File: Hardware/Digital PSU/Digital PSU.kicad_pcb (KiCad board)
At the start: 2 copper layers, 35 parts, among them J1 ACin, J2 Relay power, J3 Conn_02x09, Q1 NJW0302, Q2 MJE15030, U1 LM334Z

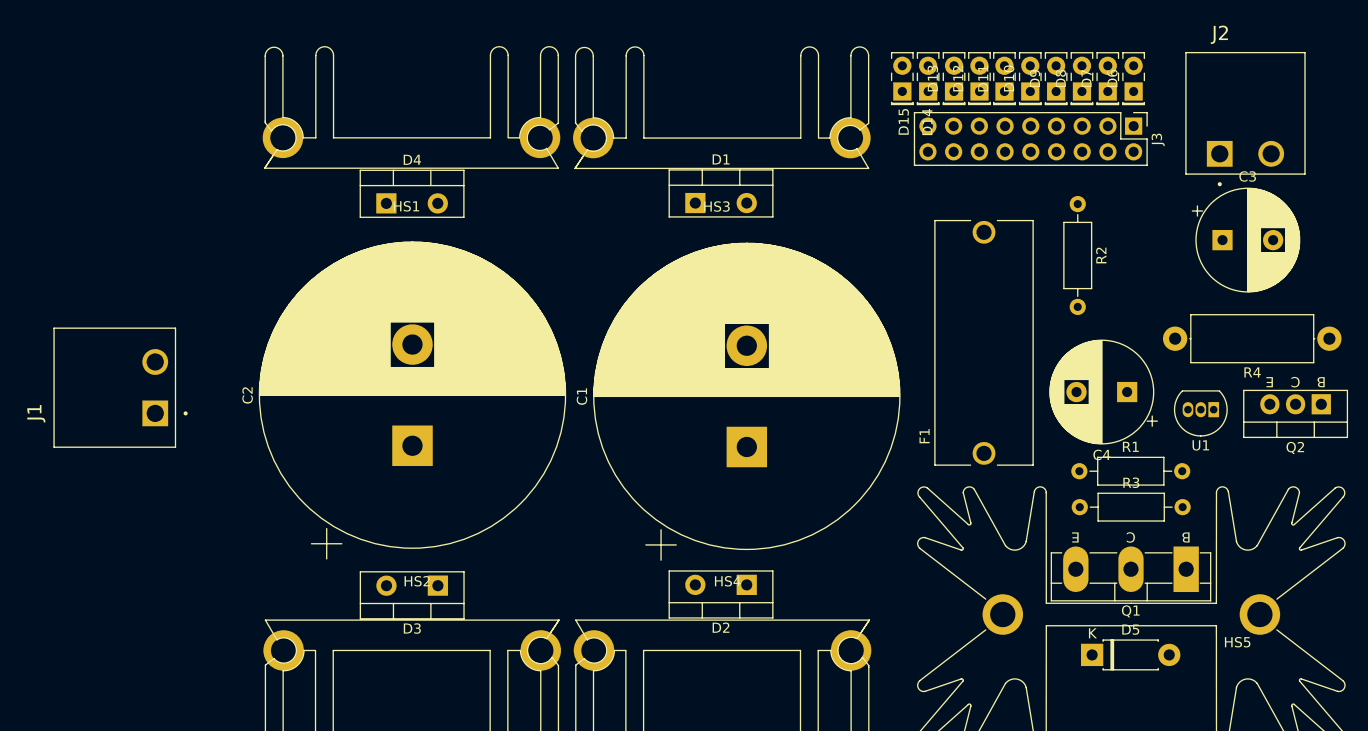
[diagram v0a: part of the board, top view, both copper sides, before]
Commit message: More work on PSU
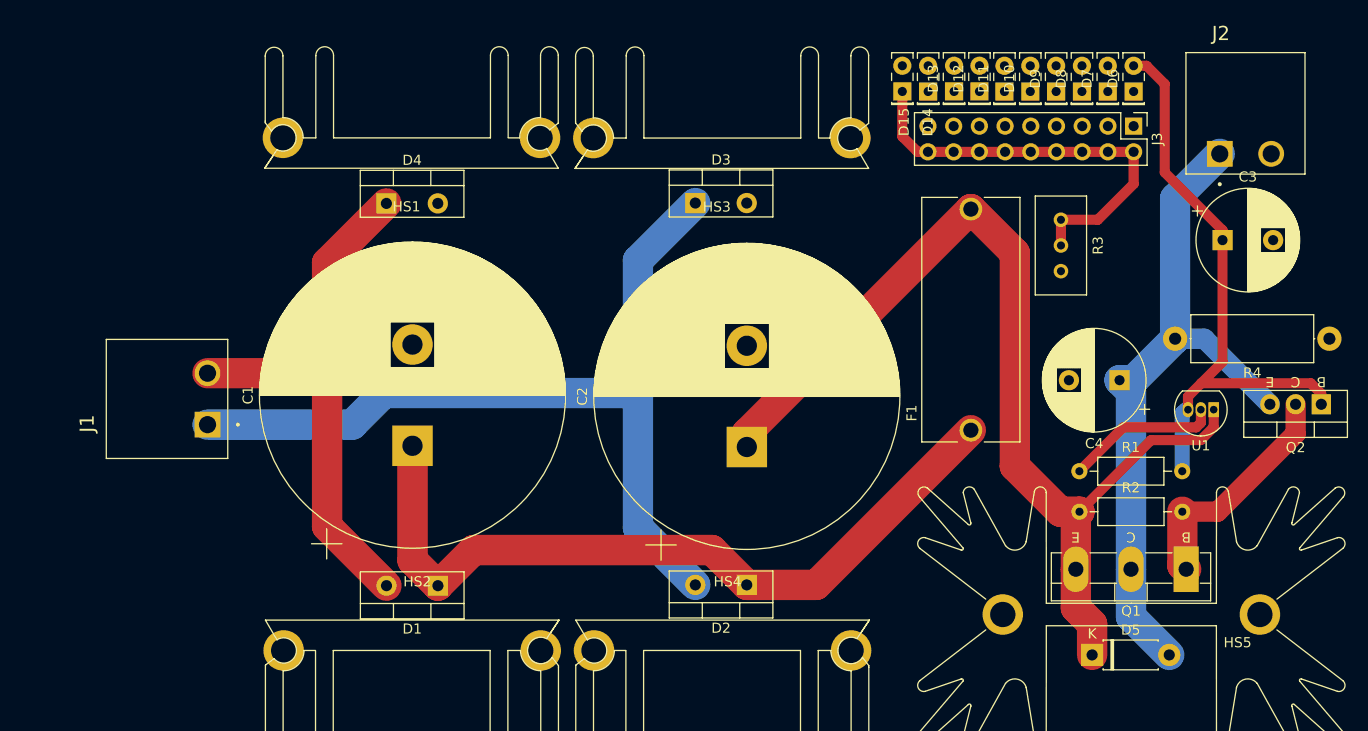
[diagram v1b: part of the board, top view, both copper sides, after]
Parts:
- R3: footprint Resistor_THT:R_Axial_DIN0207_L6.3mm_D2.5mm_P10.16mm_Horizontal -> Potentiometer_THT:Potentiometer_Bourns_3296W_Vertical
- moved D1 45.6 mm to (92.9, 165.8), turned to 180 degrees
- moved D3 45.6 mm to (118.3, 128.0), turned to 0 degrees
- moved C1 33.0 mm to (90.4, 152.0)
- moved C2 33.0 mm to (123.4, 152.1)
- moved R2 30.4 mm to (156.3, 158.5), turned to 0 degrees
- moved R3 23.4 mm to (154.4, 134.8), turned to -90 degrees
- moved J1 5.28 mm to (70.1, 149.9)
- moved F1 2.63 mm to (145.6, 139.6)
- moved C4 1.39 mm to (160.2, 145.5)
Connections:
- R3 pad 1: Net-(D15-K) -> GND
- R3 pad 2: GND -> Net-(D15-K)
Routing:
- net Net-(D5-K): track 0.00 -> 101.5 mm
- net Net-(D2-A): track 0.00 -> 86.2 mm
- net Net-(D1-K): track 0.00 -> 76.7 mm
- net +12V: track 0.00 -> 68.5 mm
- net Net-(D6-A): track 0.00 -> 59.3 mm
- net Net-(D1-A): track 0.00 -> 54.4 mm
- net Net-(D15-K): track 0.00 -> 42.3 mm
- net Net-(Q1-B): track 0.00 -> 23.1 mm
- net Net-(R1-Pad1): track 0.00 -> 15.3 mm

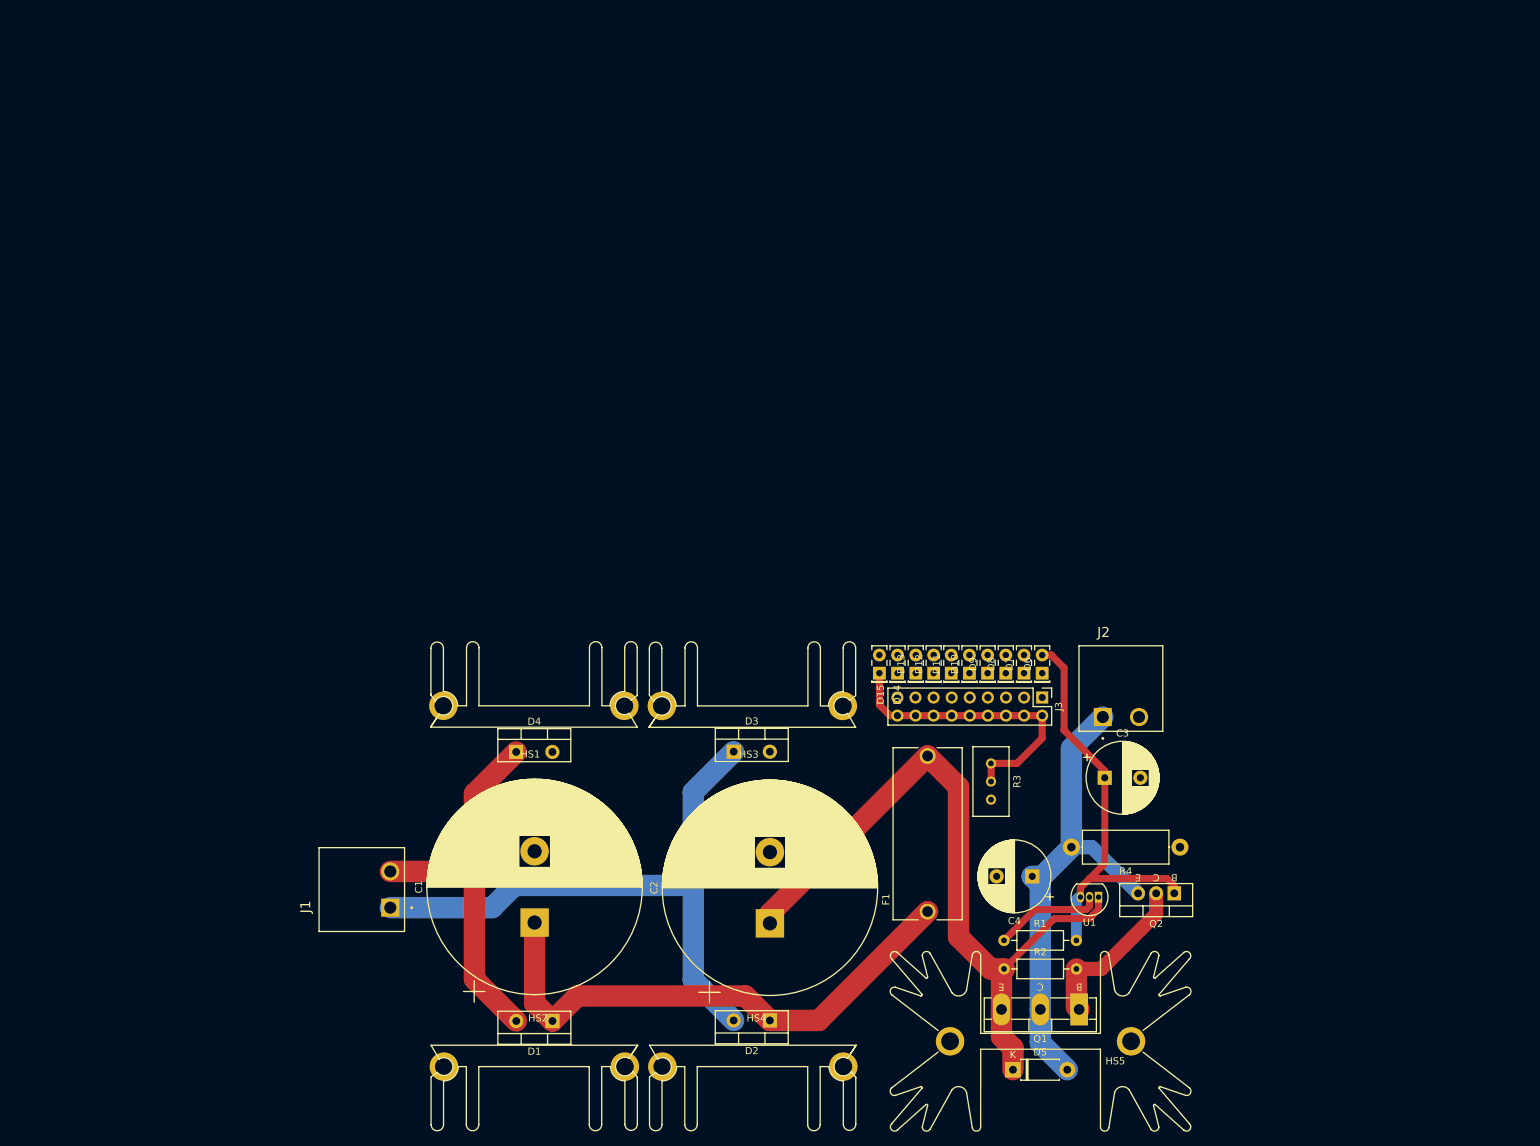
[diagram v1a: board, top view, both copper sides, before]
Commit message: Added transformer for Digital PSU
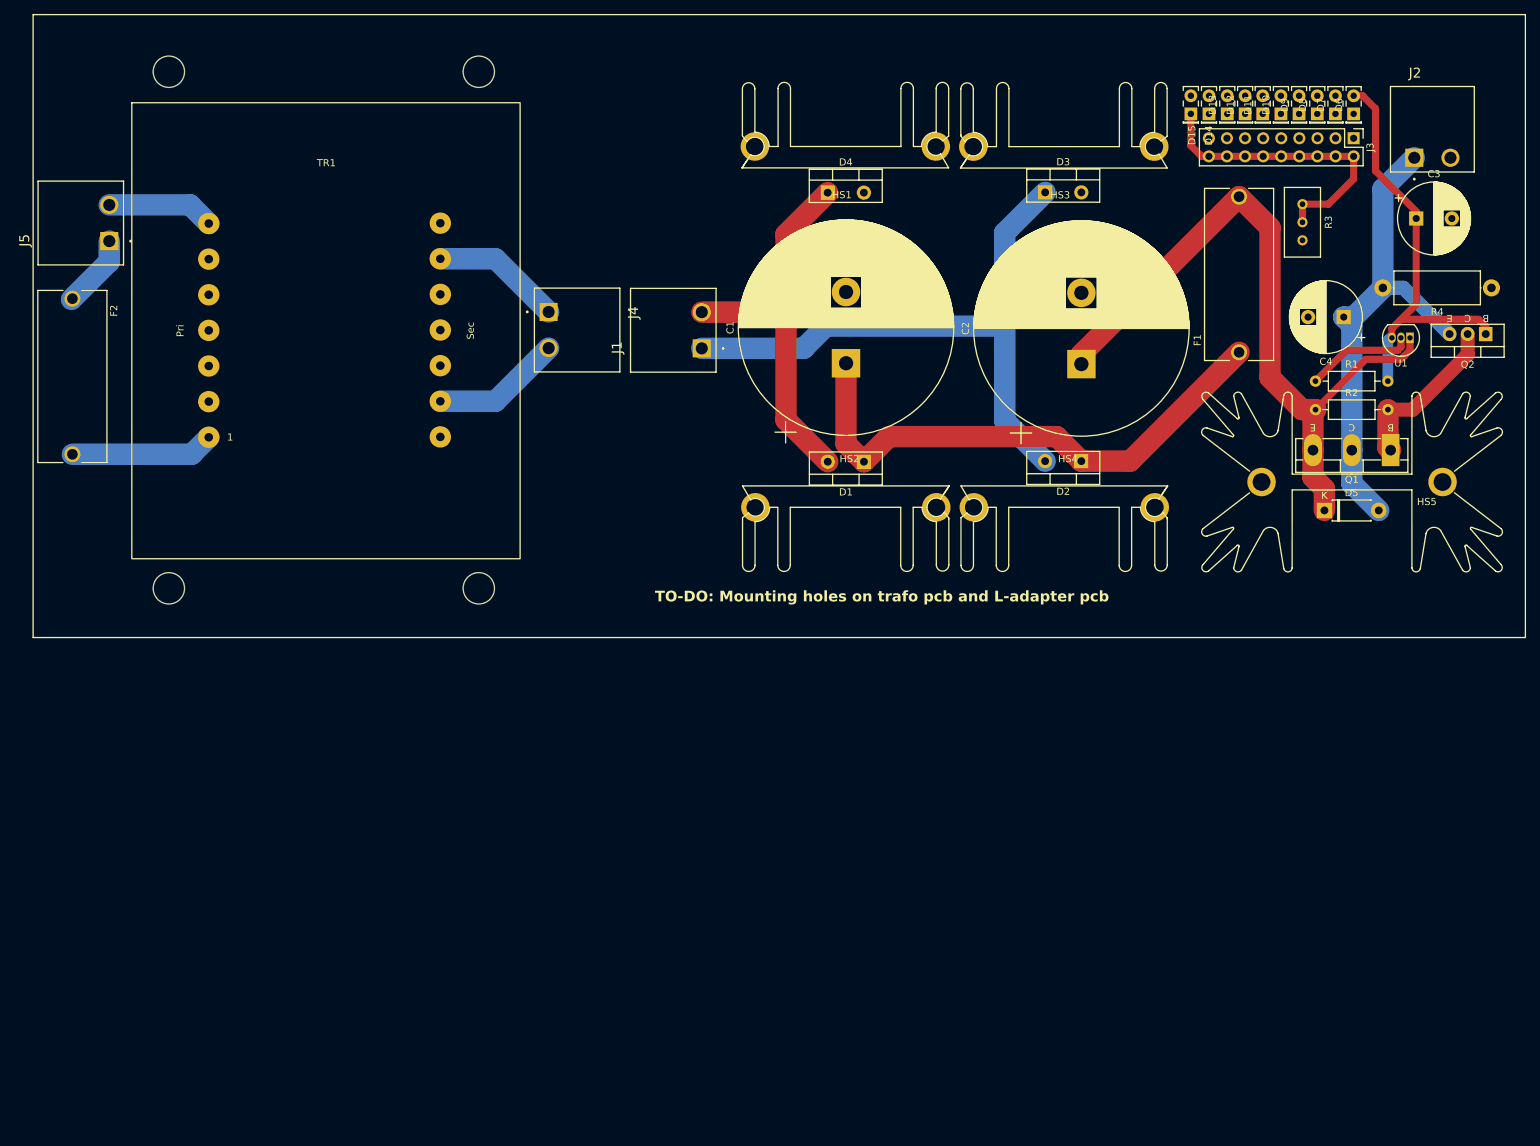
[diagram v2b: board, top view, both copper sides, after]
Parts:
- added F2: Fuse - 8A T, ThePreAmp_PSU_Fuseholder:Keystone fuseholder 4527, F.Cu at (25.5, 75.4)
- added J4: 15V AC, THE_PREAMP_CONN_POWER_5_08:TBP01R1-508-02BK, F.Cu at (92.4, 66.3)
- added J5: 230V AC, THE_PREAMP_CONN_POWER_5_08:TBP01R1-508-02BK, F.Cu at (30.7, 56.4)
- added TR1: Hahn BV EL 603 1027, Transformer_Hahn_BV_EL_603_1027:Transformer_Hahn_BV_EL_603_1027, F.Cu at (45.8, 83.9)
- J1: value ACin -> AC in
- moved HS2 89.8 mm to (134.1, 93.7)
- moved HS4 89.8 mm to (164.7, 93.7)
- moved C1 89.8 mm to (134.1, 73.5)
- moved C2 89.8 mm to (167.1, 73.6)
- moved D1 89.8 mm to (136.6, 87.3)
- moved D10 89.8 mm to (195.1, 38.5)
- moved D11 89.8 mm to (192.6, 38.5)
- moved D12 89.8 mm to (190.1, 38.5)
- moved D13 89.8 mm to (187.6, 38.5)
- moved D15 89.8 mm to (182.5, 38.5)
- moved D3 89.8 mm to (162.0, 49.5)
- moved D5 89.8 mm to (201.2, 94.2)
- moved D6 89.8 mm to (205.3, 38.5)
- moved D7 89.8 mm to (202.8, 38.5)
- moved D8 89.8 mm to (200.2, 38.5)
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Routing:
- net Net-(F2-Pad2): track 0.00 -> 20.1 mm
- net Net-(J4-Pin_2): track 0.00 -> 18.3 mm
- net Net-(J4-Pin_1): track 0.00 -> 18.3 mm
- net Net-(J5-Pin_2): track 0.00 -> 15.0 mm
- net Net-(J5-Pin_1): track 0.00 -> 10.4 mm
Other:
- board text added: "TO-DO: Mounting holes on trafo pcb and L-adapter pcb"

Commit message: Minor updates
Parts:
- moved C3 8.89 mm to (205.3, 54.4)
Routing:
- net +12V: track 68.5 -> 80.4 mm
- net Net-(D6-A): track 59.3 -> 62.2 mm
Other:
- board outline added: 206.8 x 87.4 mm
- board text added: "TO-DO: Mounting holes on trafo pcb and L-adapter pcb + cut-outs to allow transistors to be mounted on bottom of chassis + copper fills"
- board text removed: "TO-DO: Mounting holes on trafo pcb and L-adapter pcb"
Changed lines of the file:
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@@
 		(fp_arc
 			(start -14.45 -8.074396)
-			(mid -13.587327 -8.949829)
+			(mid -13.587327 -8.949831)
 			(end -12.7 -8.099396)
 			(stroke
@@
 		(fp_arc
 			(start -9.45 -8.125)
-			(mid -8.587327 -9.000434)
+			(mid -8.587327 -9.000436)
 			(end -7.7 -8.15)
 			(stroke
@@
 			(solder_mask_margin 0.102)
 		)
+		(model "${KIPRJMOD}/Libraries/THE_PREAMP_CONN_POWER_5_08.pretty/CUI_DEVICES_TBP01R1-508-02BK.step"
+			(offset
+				(xyz 5.1 19 -0.1)
+			)
+			(scale
+				(xyz 1 1 1)
+			)
+			(rotate
+				(xyz -90 0 90)
+			)
+		)
 	)
 	(footprint "Capacitor_THT:CP_Radial_D10.0mm_P5.00mm"
 		(layer "F.Cu")
-		(at 214.127323 53.202916)
+		(at 205.32 54.41)
 		(descr "CP, Radial series, Radial, pin pitch=5.00mm, , diameter=10mm, Electrolytic Capacitor")
 		(tags "CP Radial series Radial pin pitch 5.00mm  diameter 10mm Electrolytic Capacitor")
@@
 			(solder_mask_margin 0.102)
 		)
+		(model "${KIPRJMOD}/Libraries/THE_PREAMP_CONN_POWER_5_08.pretty/CUI_DEVICES_TBP01R1-508-02BK.step"
+			(offset
+				(xyz 5.1 19 -0.1)
+			)
+			(scale
+				(xyz 1 1 1)
+			)
+			(rotate
+				(xyz -90 0 90)
+			)
+		)
 	)
 	(footprint "LED_THT:LED_Rectangular_W5.0mm_H2.0mm"
@@
 		(fp_arc
 			(start -9.45 -8.125)
-			(mid -8.587327 -9.000434)
+			(mid -8.587327 -9.000436)
 			(end -7.7 -8.15)
 			(stroke
@@
 		(fp_arc
 			(start -14.45 -8.074396)
-			(mid -13.587327 -8.949829)
+			(mid -13.587327 -8.949831)
 			(end -12.7 -8.099396)
 			(stroke
@@
 		(fp_arc
 			(start -9.45 -8.125)
-			(mid -8.587327 -9.000434)
+			(mid -8.587327 -9.000436)
 			(end -7.7 -8.15)
 			(stroke
@@
 		(fp_arc
 			(start -14.45 -8.074396)
-			(mid -13.587327 -8.949829)
+			(mid -13.587327 -8.949831)
 			(end -12.7 -8.099396)
 			(stroke
@@
 			(solder_mask_margin 0.102)
 		)
+		(model "${KIPRJMOD}/Libraries/THE_PREAMP_CONN_POWER_5_08.pretty/CUI_DEVICES_TBP01R1-508-02BK.step"
+			(offset
+				(xyz 5.1 19 -0.1)
+			)
+			(scale
+				(xyz 1 1 1)
+			)
+			(rotate
+				(xyz -90 0 90)
+			)
+		)
 	)
 	(footprint "Package_TO_SOT_THT:TO-220-2_Vertical"
@@
 			(pintype "passive")
 		)
-		(model "${KICAD6_3DMODEL_DIR}/Package_TO_SOT_THT.3dshapes/TO-3P-3_Vertical.wrl"
+		(model "${KICAD8_3DMODEL_DIR}/Package_TO_SOT_THT.3dshapes/TO-3P-3_Vertical.step"
 			(offset
-				(xyz 0 0 0)
+				(xyz 0 0 6)
 			)
 			(scale
@@
 			(pintype "passive")
 		)
-		(model "${KICAD6_3DMODEL_DIR}/Package_TO_SOT_THT.3dshapes/TO-220-3_Vertical.wrl"
+		(model "${KICAD8_3DMODEL_DIR}/Package_TO_SOT_THT.3dshapes/TO-220-2_Vertical.wrl"
 			(offset
-				(xyz 0 0 0)
+				(xyz 0 0 3.5)
 			)
 			(scale
@@
 		(fp_arc
 			(start -14.45 -8.074396)
-			(mid -13.587327 -8.949829)
+			(mid -13.587327 -8.949831)
 			(end -12.7 -8.099396)
 			(stroke
@@
 		(fp_arc
 			(start -9.45 -8.125)
-			(mid -8.587327 -9.000434)
+			(mid -8.587327 -9.000436)
 			(end -7.7 -8.15)
 			(stroke
@@
 		(at 30.6975 56.38 90)
 		(property "Reference" "J5"
-			(at 0.105 -11.889 270)
+			(at 0.105 -11.889 -90)
 			(layer "F.SilkS")
 			(effects
@@
 		)
 		(property "Value" "230V AC"
-			(at 13.44 3.361 270)
+			(at 13.44 3.361 -90)
 			(layer "F.Fab")
 			(effects
@@
 			(solder_mask_margin 0.102)
 		)
+		(model "${KIPRJMOD}/Libraries/THE_PREAMP_CONN_POWER_5_08.pretty/CUI_DEVICES_TBP01R1-508-02BK.step"
+			(offset
+				(xyz 5.1 19 -0.1)
+			)
+			(scale
+				(xyz 1 1 1)
+			)
+			(rotate
+				(xyz -90 0 90)
+			)
+		)
 	)
 	(footprint "LED_THT:LED_Rectangular_W5.0mm_H2.0mm"
@@
 		)
 	)
+	(gr_line
+		(start 103.19 17.75)
+		(end 103.19 130.67)
+		(stroke
+			(width 0.2)
+			(type default)
+		)
+		(layer "B.Cu")
+	)
 	(gr_rect
-		(start 20.01 24.59)
-		(end 229.45 112.02)
+		(start 20.33 24.62)
+		(end 227.11 112.01)
 		(stroke
-			(width 0.1)
+			(width 0.05)
 			(type default)
 		)
 		(fill none)
-		(layer "F.SilkS")
+		(layer "Edge.Cuts")
 	)
-	(gr_text "TO-DO: Mounting holes on trafo pcb and L-adapter pcb"
-		(at 107.28 107.13 -0)
+	(gr_text "TO-DO: Mounting holes on trafo pcb and L-adapter pcb + cut-outs to allow transistors to be mounted on bottom of chassis + copper fills"
+		(at 44.88 110.81 0)
 		(layer "F.SilkS")
 		(effects
@@
 	)
 	(segment
-		(start 203.952677 67.042916)
-		(end 205.345 67.042916)
+		(start 212.2125 62.942916)
+		(end 218.6925 69.422916)
 		(width 3)
 		(layer "B.Cu")
@@
 	)
 	(segment
-		(start 205.085 85.717916)
-		(end 205.085 68.175239)
+		(start 209.445 62.942916)
+		(end 212.2125 62.942916)
 		(width 3)
 		(layer "B.Cu")
@@
 	)
 	(segment
-		(start 209.445 62.942916)
-		(end 209.445 49.090416)
+		(start 203.952677 67.042916)
+		(end 205.345 67.042916)
+		(width 3)
+		(layer "B.Cu")
+		(net 2)
+	)
+	(segment
+		(start 205.085 85.717916)
+		(end 205.085 68.175239)
 		(width 3)
 		(layer "B.Cu")
@@
 	)
 	(segment
-		(start 209.445 49.090416)
-		(end 213.855 44.680416)
+		(start 213.855 44.680416)
+		(end 213.855 58.532916)
+		(width 3)
+		(layer "B.Cu")
+		(net 2)
+	)
+	(segment
+		(start 213.855 58.532916)
+		(end 209.445 62.942916)
 		(width 3)
 		(layer "B.Cu")
@@
 	)
 	(segment
-		(start 214.127323 53.202916)
-		(end 214.127323 52.225239)
+		(start 210.715 69.952916)
+		(end 210.715 68.045)
 		(width 1)
 		(layer "F.Cu")
@@
 	)
 	(segment
-		(start 212.015 67.352916)
-		(end 214.127323 65.240593)
+		(start 210.715 68.045)
+		(end 205.32 62.65)
 		(width 1)
 		(layer "F.Cu")
@@
 	)
 	(segment
-		(start 210.715 68.652916)
-		(end 210.715 69.952916)
+		(start 205.32 62.65)
+		(end 205.32 54.41)
 		(width 1)
 		(layer "F.Cu")
@@
 	)
 	(segment
-		(start 208.415 37.780124)
-		(end 206.617792 35.982916)
+		(start 210.715 68.652916)
+		(end 210.715 69.952916)
 		(width 1)
 		(layer "F.Cu")
@@
 	)
 	(segment
-		(start 214.127323 52.225239)
-		(end 208.415 46.512916)
+		(start 208.415 37.780124)
+		(end 206.617792 35.982916)
 		(width 1)
 		(layer "F.Cu")
@@
 	)
 	(segment
-		(start 214.127323 65.240593)
-		(end 214.127323 53.202916)
+		(start 205.32 49.607916)
+		(end 208.415 46.512916)
 		(width 1)
 		(layer "F.Cu")
@@
 		(width 1)
 		(layer "F.Cu")
+		(net 4)
+	)
+	(segment
+		(start 205.32 54.41)
+		(end 205.32 49.607916)
+		(width 1)
+		(layer "F.Cu")

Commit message: Pcb dimensions
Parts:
- added C5: 330nF, Capacitor_SMD:C_0805_2012Metric_Pad1.18x1.45mm_HandSolder, F.Cu at (245.6, 66.6)
- added C6: 100nF, Capacitor_SMD:C_0805_2012Metric_Pad1.18x1.45mm_HandSolder, F.Cu at (245.6, 91.9)
- added C7: 10nF, Capacitor_SMD:C_0805_2012Metric_Pad1.18x1.45mm_HandSolder, F.Cu at (245.6, 60.1)
- added C8: 10uF 16V, Capacitor_SMD:C_1206_3216Metric_Pad1.33x1.80mm_HandSolder, F.Cu at (245.6, 98.4)
- added HS6: Heatsink, ThePreAmp_PSU_Heatsinks:Heatsink_Fischer_SK145-STS_29x12mm_2xDrill2.5mm, F.Cu at (237.4, 63.9)
- added HS7: Heatsink, ThePreAmp_PSU_Heatsinks:Heatsink_Fischer_SK145-STS_29x12mm_2xDrill2.5mm, F.Cu at (237.4, 95.4)
- added J6: ESP32 power, THE_PREAMP_CONN_POWER_5_08:TBP01R1-508-02BK, F.Cu at (251.3, 61.3)
- added J7: Opt. 3V3 power, THE_PREAMP_CONN_POWER_5_08:TBP01R1-508-02BK, F.Cu at (251.3, 92.9)
- added J8: DC in, THE_PREAMP_CONN_POWER_5_08:TBP01R1-508-02BK, F.Cu at (237.8, 43.0)
- added J9: Relay power, THE_PREAMP_CONN_POWER_5_08:TBP01R1-508-02BK, F.Cu at (251.3, 38.0)
- added U2: LM7808_TO220, Package_TO_SOT_THT:TO-220-3_Vertical, F.Cu at (240.9, 66.4)
- added U3: LD1117V33, Package_TO_SOT_THT:TO-220-3_Vertical, F.Cu at (240.9, 97.9)
- moved J2 7.33 mm to (216.8, 38.0), turned to -90 degrees
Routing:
- net +12V: track 80.4 -> 178.0 mm
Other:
- board size 206.8 x 87.4 mm -> 241.4 x 87.4 mm
